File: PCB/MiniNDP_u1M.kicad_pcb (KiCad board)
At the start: 2 copper layers, 51.3 x 18.3 mm, 15 parts, among them J1 Model_100_System_BUS, U1 AS6C8008_TSOPII, U2 HC238, U3 HC4040, U4 ABT841

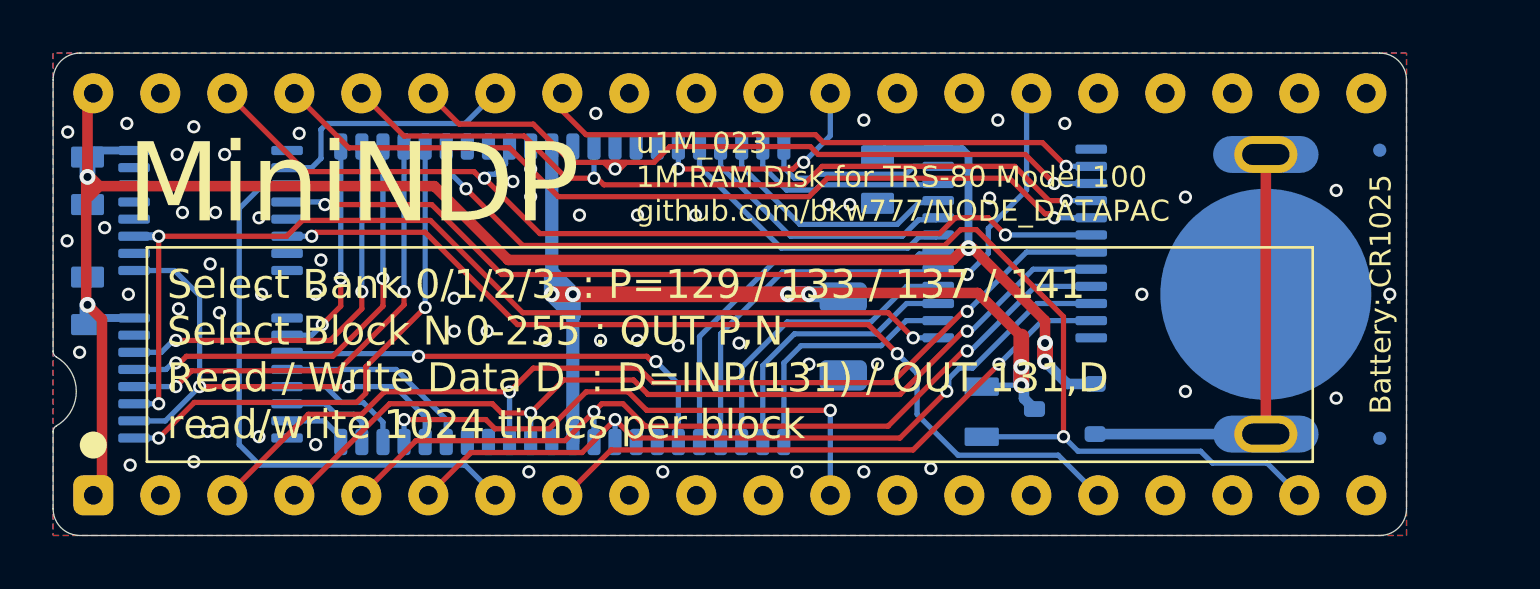
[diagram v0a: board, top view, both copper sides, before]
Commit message: minindp ez1m sl1m ez512 u1m pcbs trace spacing & gnd paths
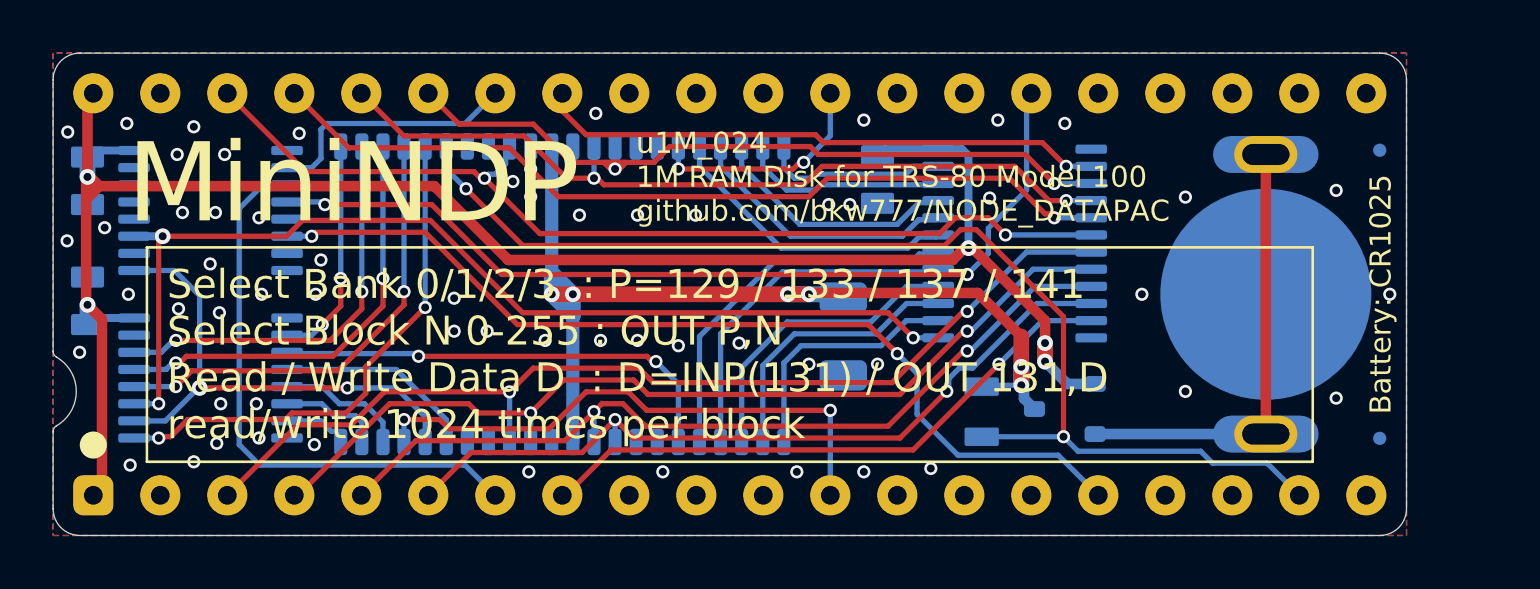
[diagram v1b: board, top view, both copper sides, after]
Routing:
- net GND: vias 57 -> 59

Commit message: u1M fine tune traces
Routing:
- net VBUS: track 70.7 -> 71.5 mm
- net GND: vias 59 -> 58

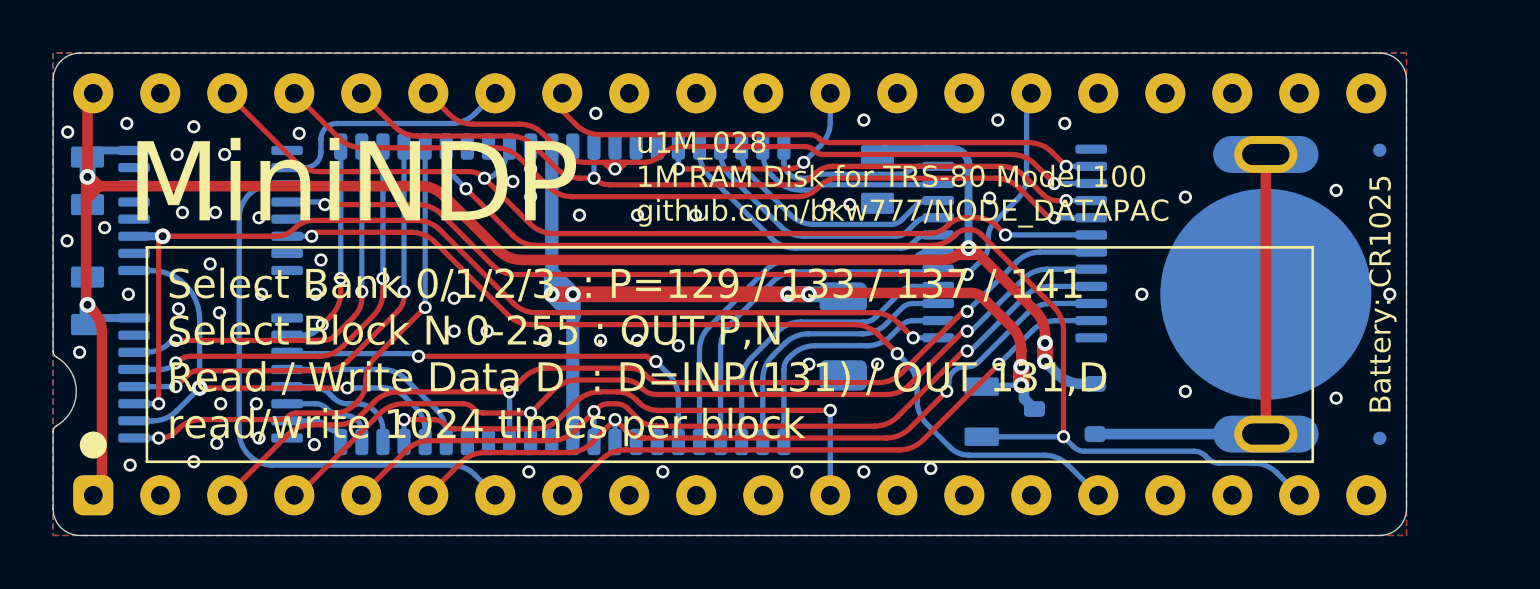
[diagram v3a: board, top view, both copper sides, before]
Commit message: u1m microscopic trace spacing/curves adjustments
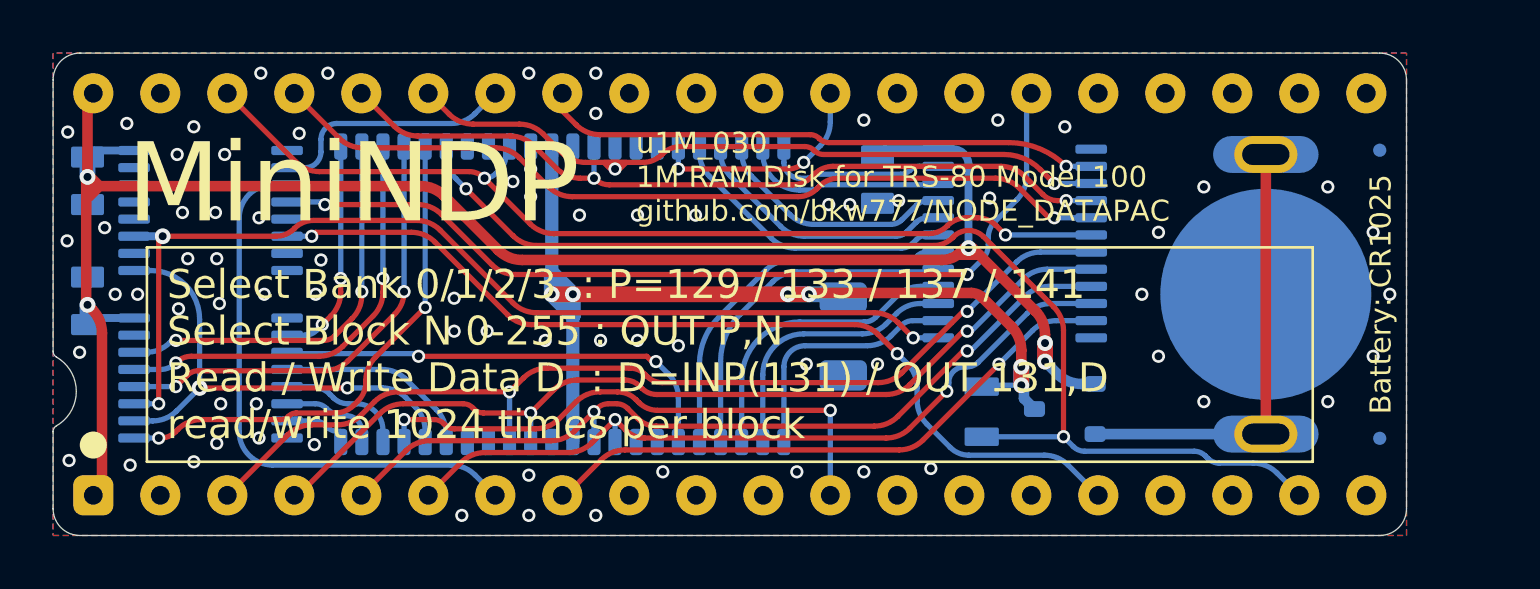
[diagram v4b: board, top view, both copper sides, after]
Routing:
- net GND: vias 58 -> 73

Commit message: u1m microscopic trace spacing/curves adjustments
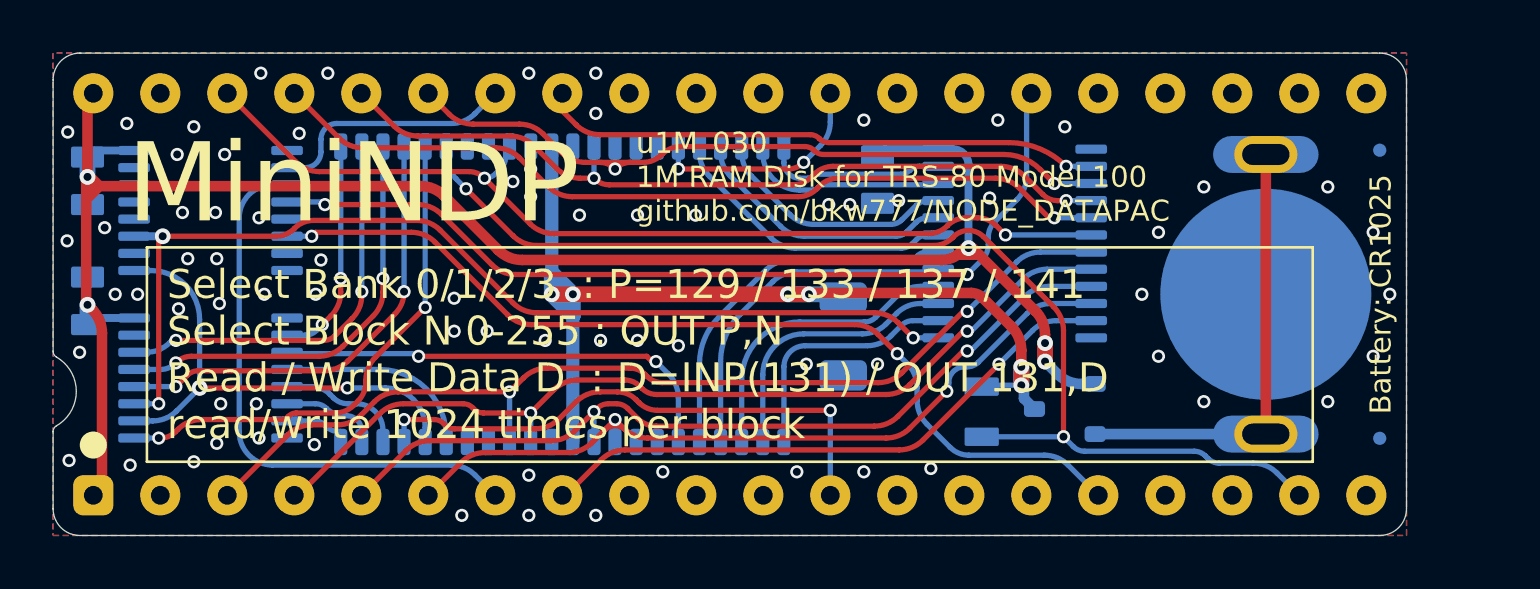
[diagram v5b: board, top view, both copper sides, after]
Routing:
- net /AD7: track 27.5 -> 28.8 mm

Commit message: Olivetti M-10 take 3. T512 pics readme.
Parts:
- U4: footprint 000_LOCAL:TSSOP-24_4.4x7.8mm_P0.65mm -> 000_LOCAL:TSSOP-24

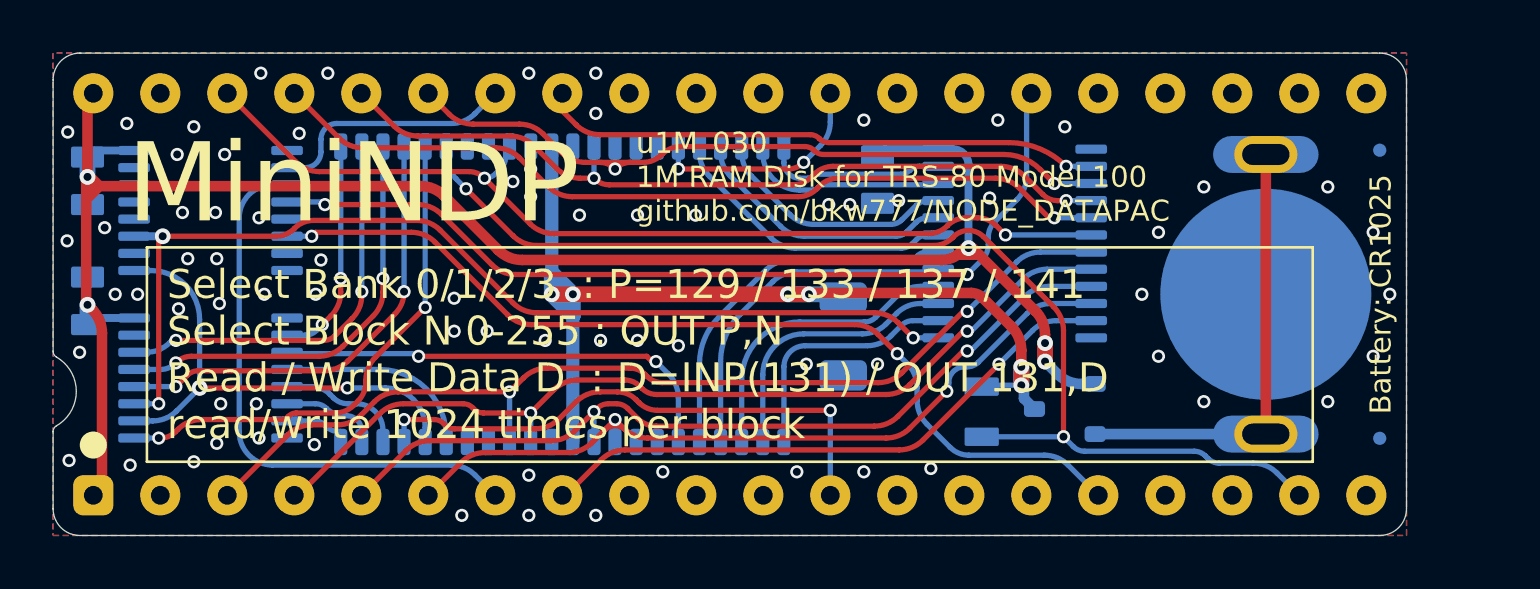
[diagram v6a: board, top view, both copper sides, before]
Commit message: u1M vias near C1 pad, silkscreen, smooth traces
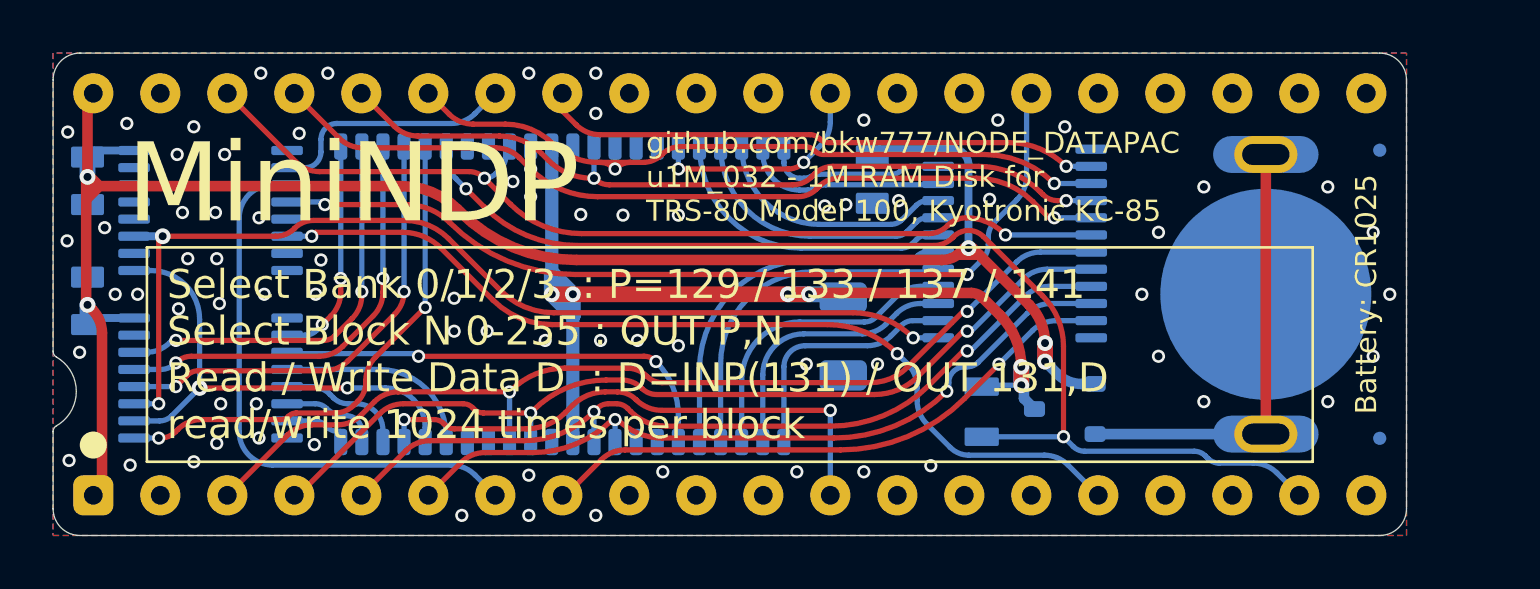
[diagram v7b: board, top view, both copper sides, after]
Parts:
- moved C1 0.20 mm to (155.4, 95.7)
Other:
- board text added: "${COMMENT1} ${REVISION} - 1M RAM Disk for TRS-80 Model 100, Kyotronic KC-85"
- board text removed: "${REVISION} ${COMMENT2} ${COMMENT1}"
